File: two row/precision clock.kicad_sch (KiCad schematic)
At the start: 41 parts, among them J2 Barrel_Jack_Switch, Q1 2N5401, Q2 2N5401

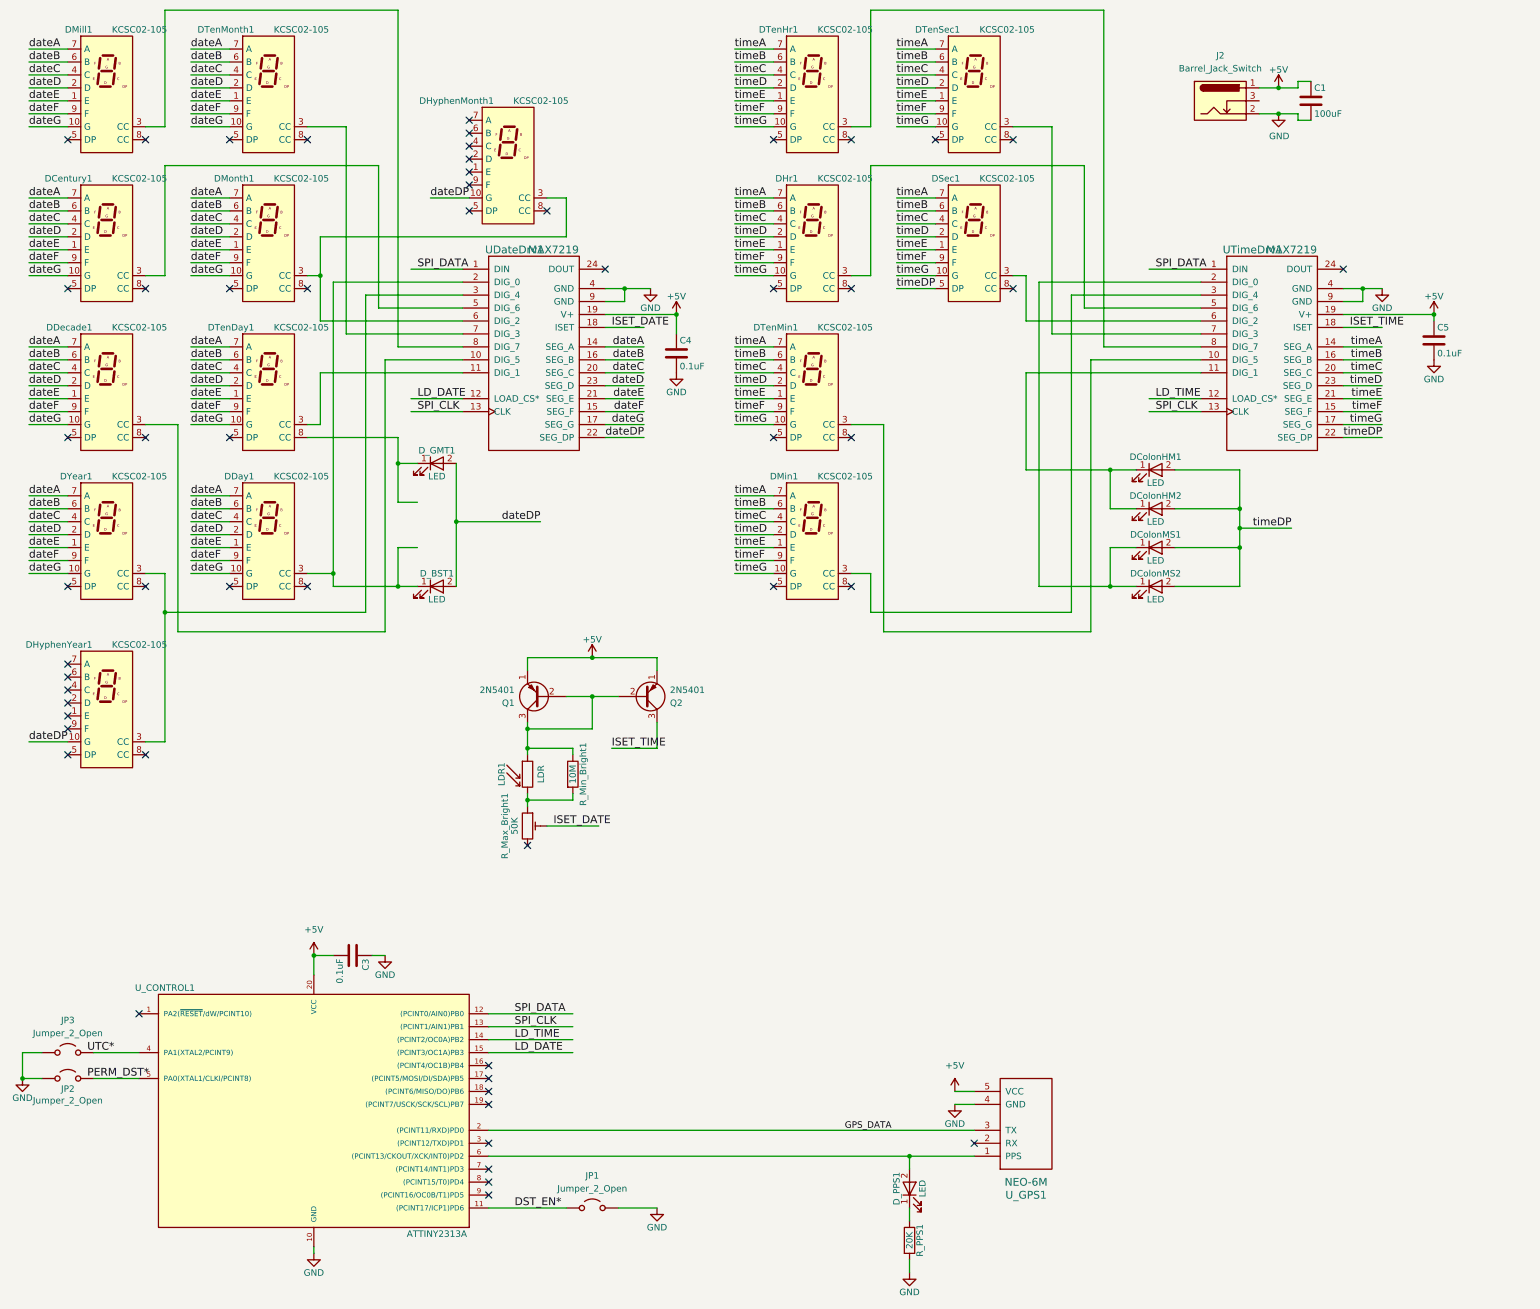
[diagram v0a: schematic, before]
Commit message: Rebuild two-row for 0.8" segments and improvements from prototype (1.0" are very difficult to source)
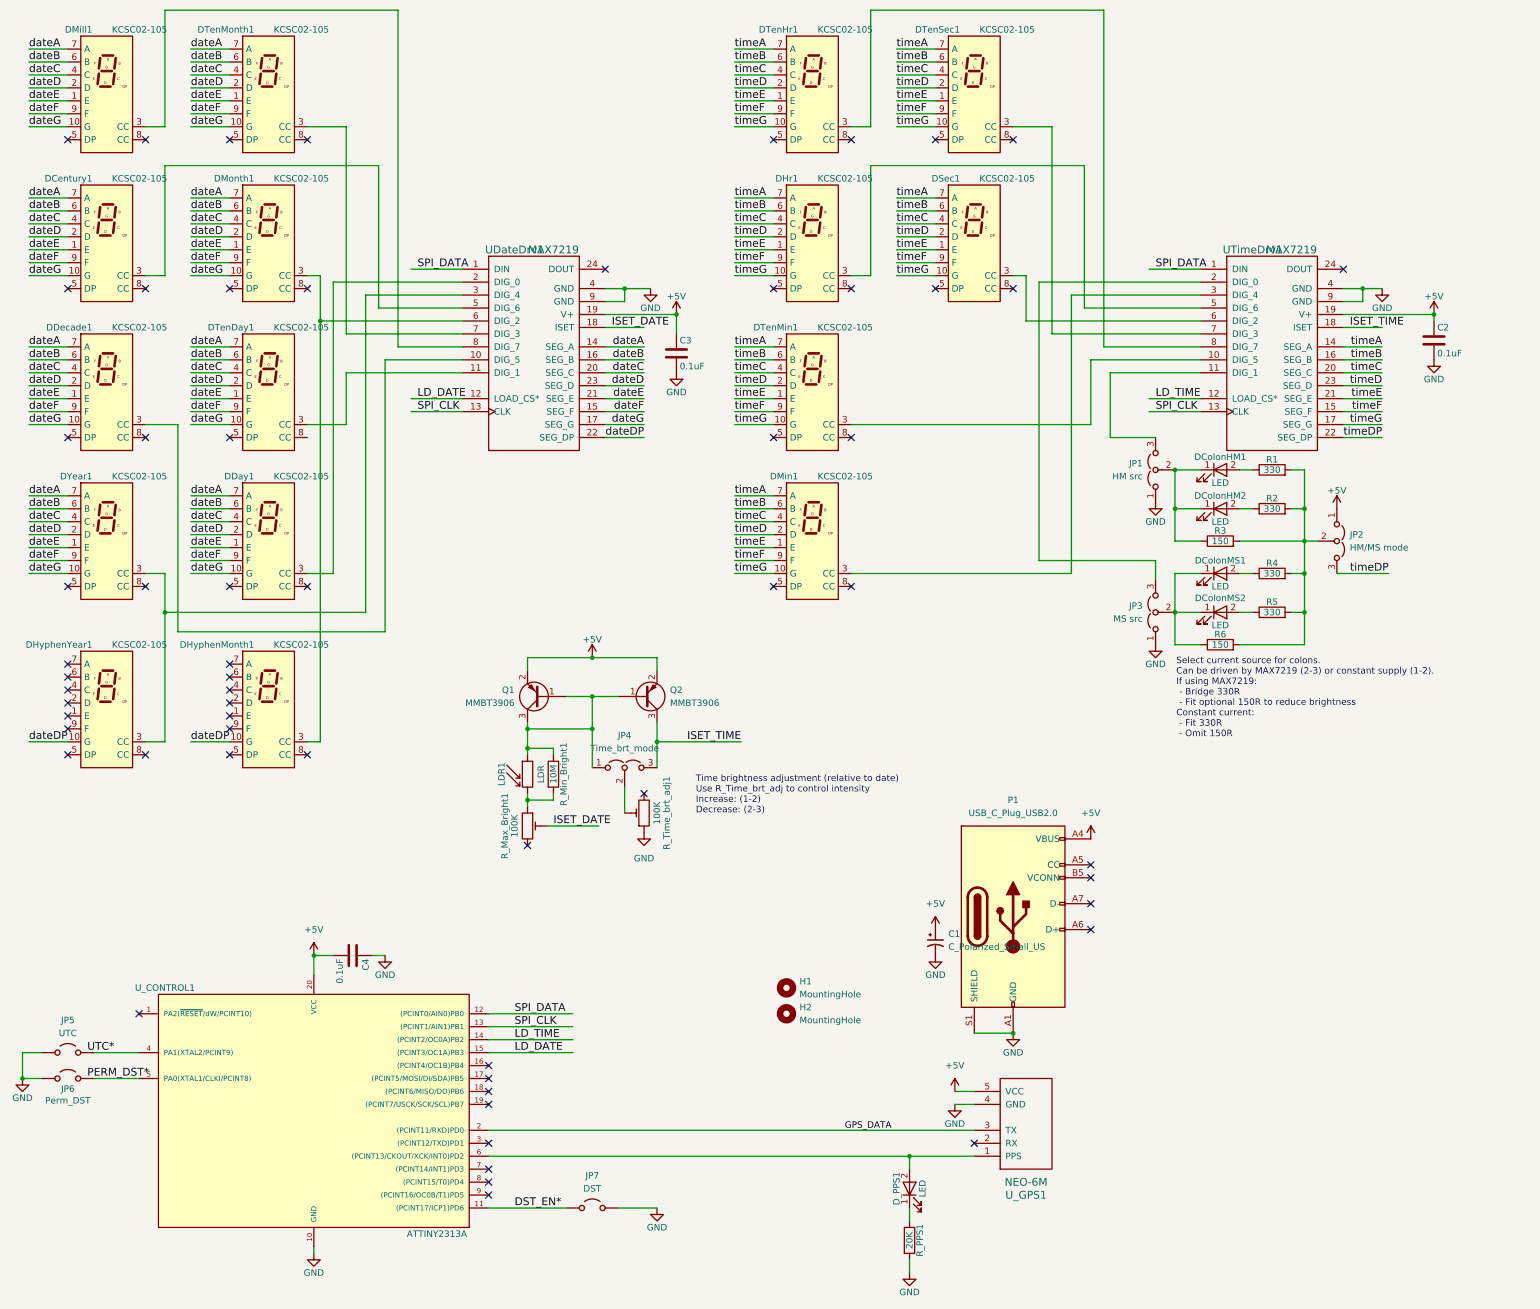
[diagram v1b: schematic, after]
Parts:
- removed C1: 100uF, Capacitor_THT:CP_Radial_D5.0mm_P2.50mm, symbol precision-clock-rescue:C
- removed D_BST1, D_GMT1: LED, LED_SMD:LED_1206_3216Metric, symbol precision-clock-rescue:LED
- removed J2: Barrel_Jack_Switch, Connector_BarrelJack:BarrelJack_Horizontal, symbol Connector:Barrel_Jack_Switch
- removed Q1, Q2: 2N5401, Package_TO_SOT_THT:TO-92_Inline_Wide, symbol precision-clock-rescue:Q_PNP_EBC
- added C1: C_Polarized_Small_US, Capacitor_THT:CP_Radial_D5.0mm_P2.50mm, symbol Device:C_Polarized_Small_US
- added H1: MountingHole, MountingHole:MountingHole_3.2mm_M3, symbol Mechanical:MountingHole
- added H2: MountingHole, MountingHole:MountingHole_2mm, symbol Mechanical:MountingHole
- added JP1: HM src, Jumper:SolderJumper-3_P1.3mm_Open_Pad1.0x1.5mm, symbol Jumper:Jumper_3_Open
- added JP2: HM/MS mode, Jumper:SolderJumper-3_P1.3mm_Open_Pad1.0x1.5mm, symbol Jumper:Jumper_3_Open
- added JP3: MS src, Jumper:SolderJumper-3_P1.3mm_Open_Pad1.0x1.5mm, symbol Jumper:Jumper_3_Open
- added JP4: Time_brt_mode, Connector_PinHeader_2.54mm:PinHeader_1x03_P2.54mm_Vertical, symbol Jumper:Jumper_3_Open
- added P1: USB_C_Plug_USB2.0, Connector_USB:USB_C_Receptacle_GCT_USB4125-xx-x_6P_TopMnt_Horizontal, symbol Connector:USB_C_Plug_USB2.0
- added Q1, Q2: MMBT3906, Package_TO_SOT_SMD:SOT-23, symbol Transistor_BJT:MMBT3906
- added R1, R2, R4, R5: 330, Resistor_SMD:R_1206_3216Metric, symbol precision-clock-rescue:R
- added R3, R6: 150, Resistor_SMD:R_1206_3216Metric, symbol precision-clock-rescue:R
- added R_Time_brt_adj1: 100K, Potentiometer_THT:Potentiometer_Piher_PT-6-V_Vertical, symbol precision-clock-rescue:POT_TRIM
- DHr1, DMin1, DSec1, DTenHr1, DTenMin1, DTenSec1: footprint precision clock:7seg1inchCC -> precision clock:7seg0.8CC
- JP5: renamed from JP3; value Jumper_2_Open -> UTC
- JP6: renamed from JP2; value Jumper_2_Open -> Perm_DST
- JP7: renamed from JP1; value Jumper_2_Open -> DST
- R_Max_Bright1: value 50K -> 100K
- U_GPS1: footprint Connector_PinHeader_2.54mm:PinHeader_1x05_P2.54mm_Vertical -> Connector_PinSocket_2.54mm:PinSocket_1x05_P2.54mm_Horizontal
- renumbered C5 to C2, C4 to C3, C3 to C4
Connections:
- net +5V: now also C1.1, JP2.1 (A), P1.A4 (VBUS), P1.A9 (VBUS), P1.B4 (VBUS), P1.B9 (VBUS), Q1.2 (E), Q2.2 (E)
- net GND: now also C1.2, JP1.1 (A), JP3.1 (A), P1.A1 (GND), P1.A12 (GND), P1.B1 (GND), P1.B12 (GND), P1.S1 (SHIELD), R_Time_brt_adj1.1
- net ISET_TIME: now also JP4.3 (B), Q2.3 (C)
- net timeDP: now also JP2.3 (B); no longer DColonHM1.2 (A), DColonHM2.2 (A), DColonMS1.2 (A), DColonMS2.2 (A), DSec1.5 (DP)
- net at DColonHM1.1 (K), DColonHM2.1 (K): now also JP1.2 (C), R3.1; no longer UTimeDrv1.11 (DIG_1)
- net at DColonMS1.1 (K), DColonMS2.1 (K): now also JP3.2 (C), R6.1; no longer UTimeDrv1.2 (DIG_0)
- net at LDR1.1, R_Min_Bright1.1: now also JP4.1 (A), Q1.1 (B), Q1.3 (C), Q2.1 (B)
- new net: JP1.3 (B), UTimeDrv1.11 (DIG_1)
- new net: JP3.3 (B), UTimeDrv1.2 (DIG_0)
- new net: DColonHM2.2 (A), R2.1
- new net: DColonMS1.2 (A), R4.1
- new net: DColonMS2.2 (A), R5.1
- new net: DColonHM1.2 (A), R1.1
- new net: JP2.2 (C), R1.2, R2.2, R3.2, R4.2, R5.2, R6.2
- new net: JP4.2 (C), R_Time_brt_adj1.2
- no-connect marks 55 -> 61
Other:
- note added: "Select current source for colons. Can be driven by MAX7219 (2-3) or constant supply (1-2). If using MAX7219: - Bridge 330R - Fit optional 150R to reduce brightness Constant current: - Fit 330R - Omit 150R"
- note added: "Time brightness adjustment (relative to date) Use R_Time_brt_adj to control intensity Increase: (1-2) Decrease: (2-3)"
- moved on the sheet: DColonHM1, DColonHM2, DColonMS1, DColonMS2, DHyphenMonth1, R_Min_Bright1

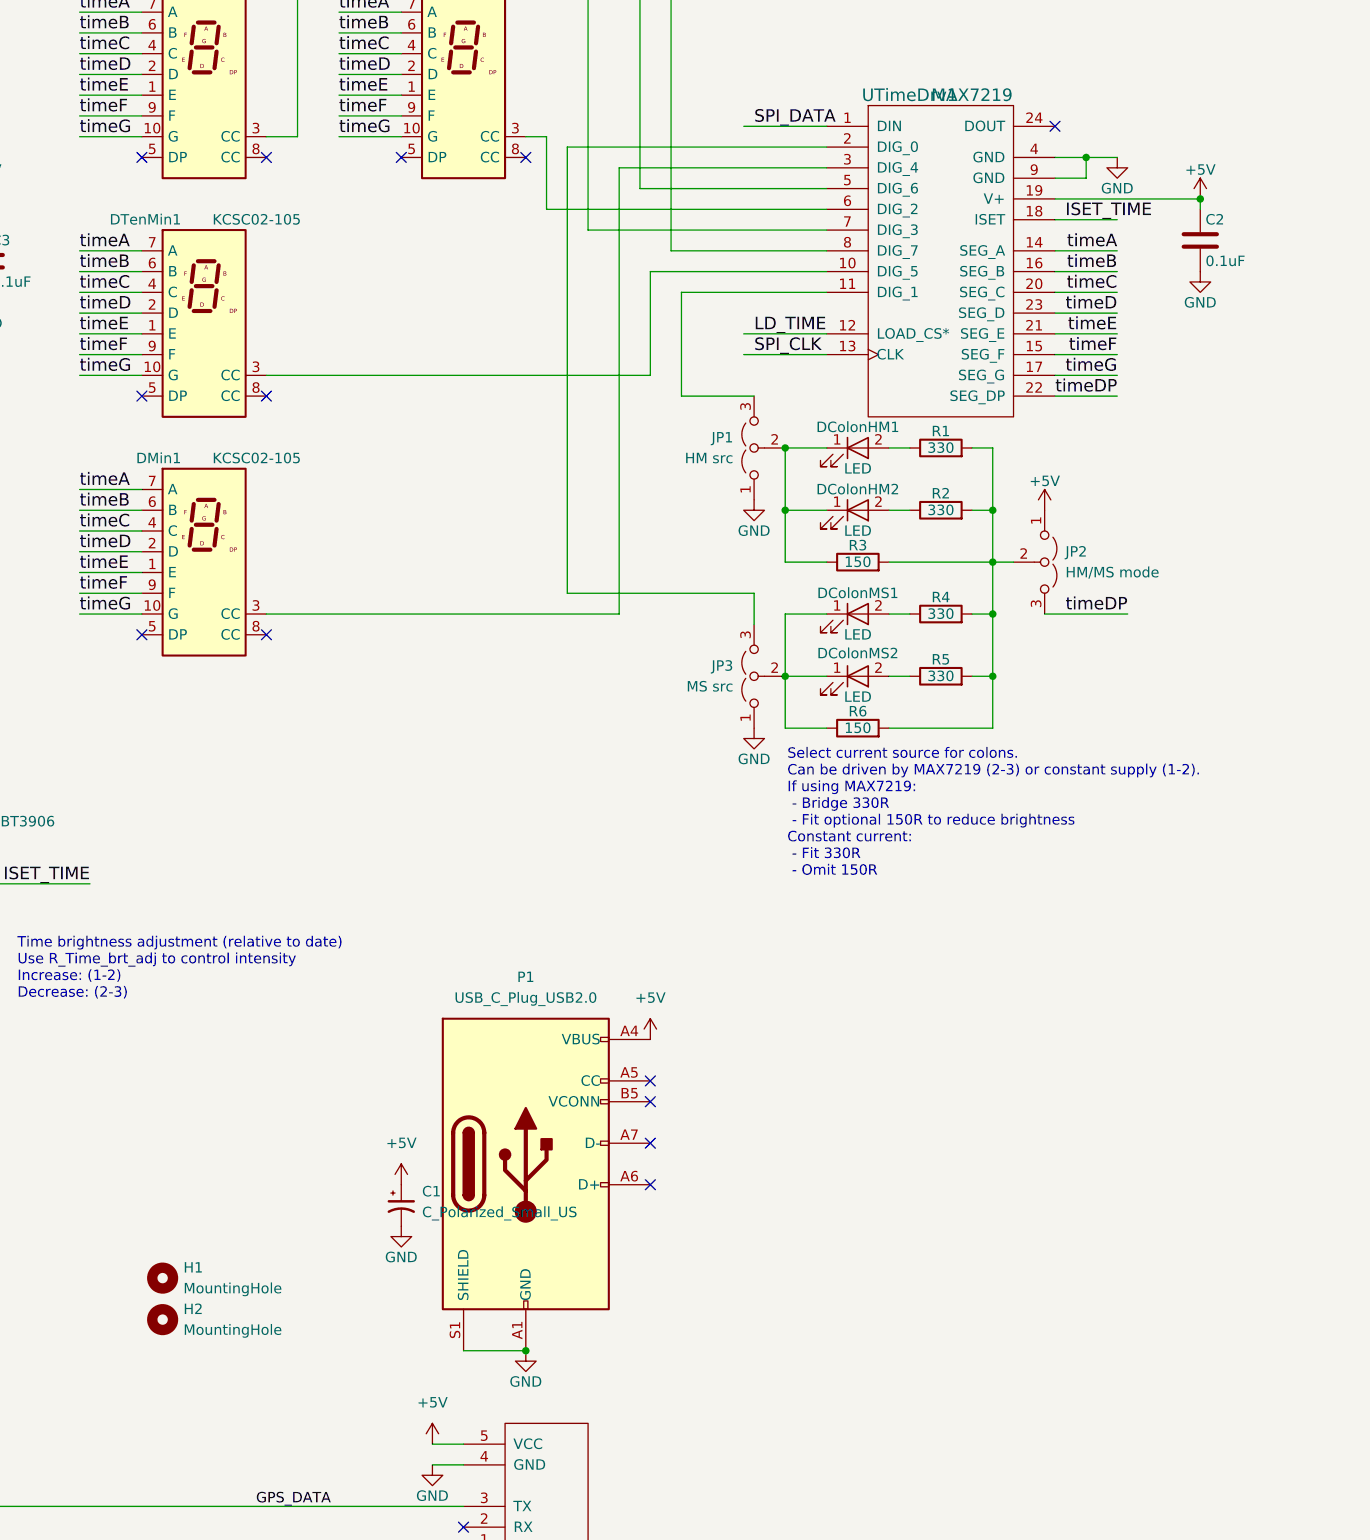
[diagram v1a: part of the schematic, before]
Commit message: Remove extra resistors, add second USB port location, cleanup trace routing
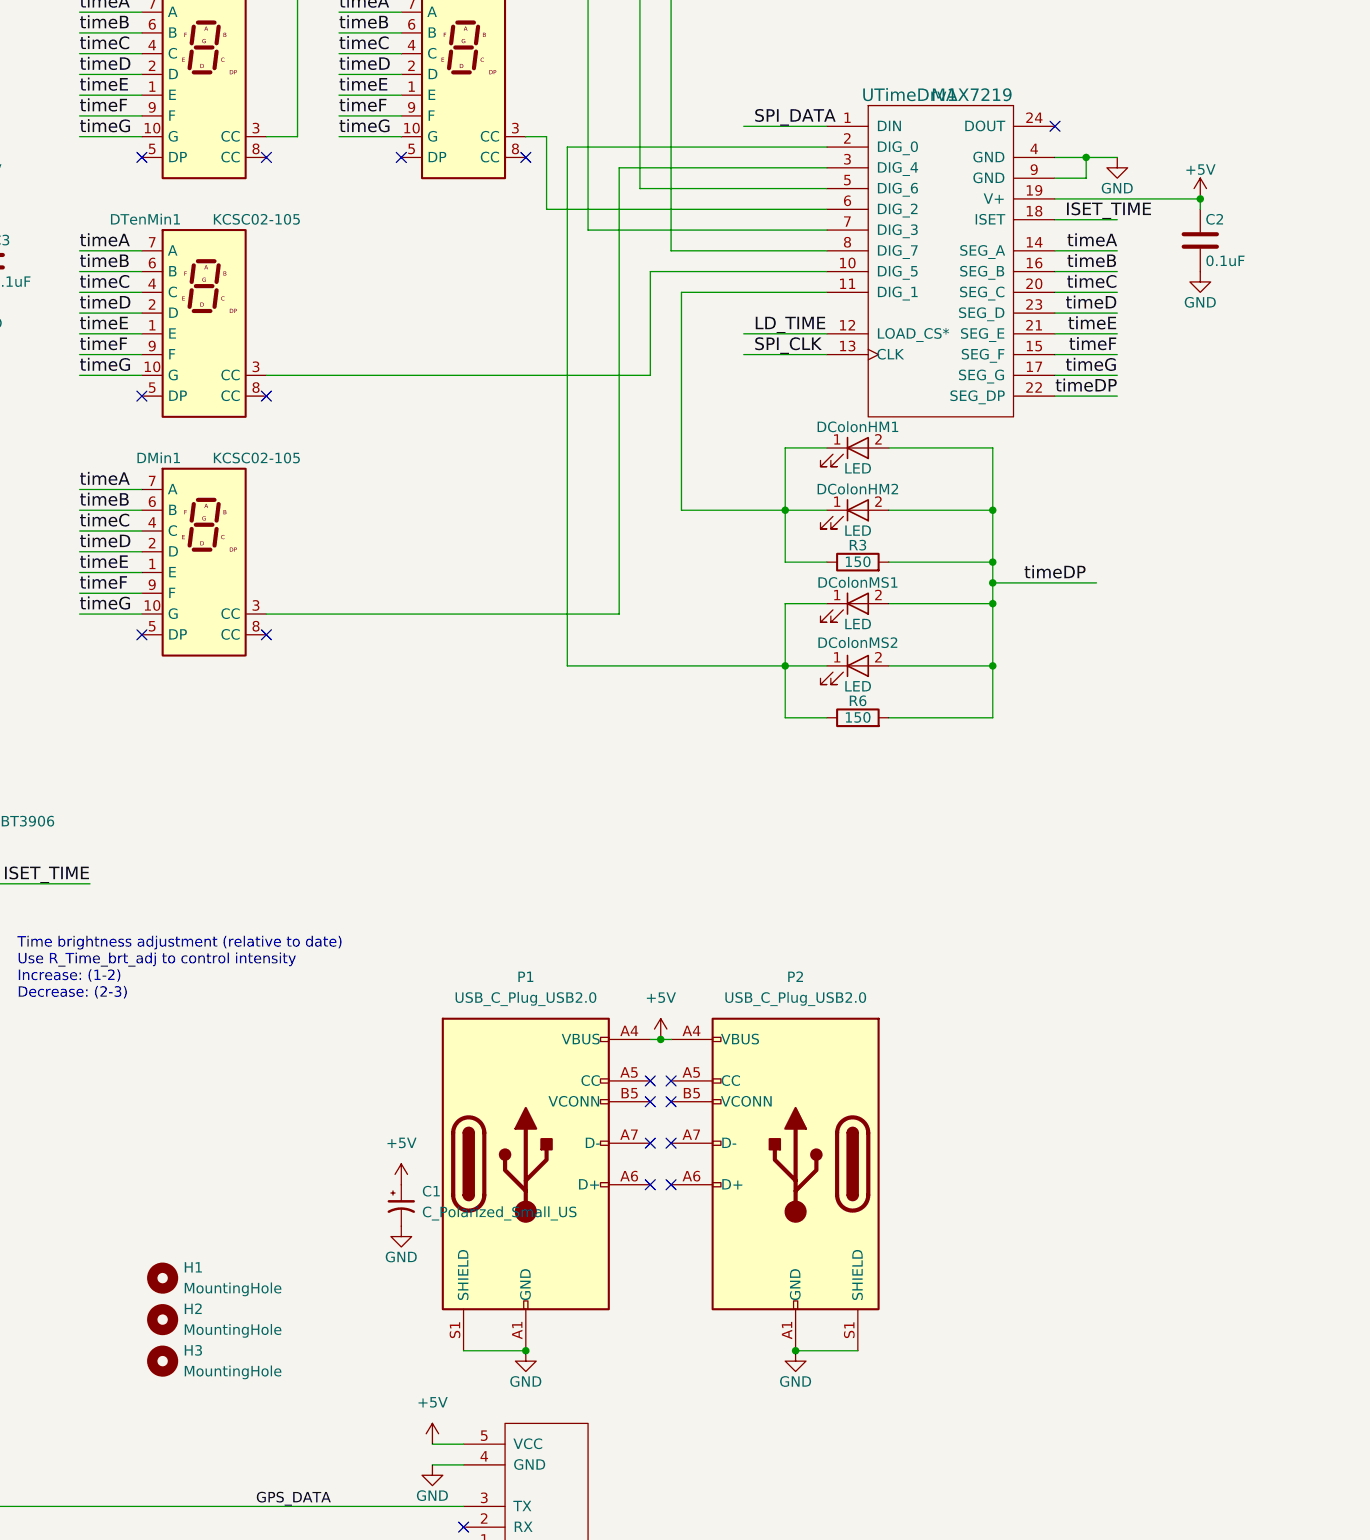
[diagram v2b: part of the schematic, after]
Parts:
- removed JP1: HM src, Jumper:SolderJumper-3_P1.3mm_Open_Pad1.0x1.5mm, symbol Jumper:Jumper_3_Open
- removed JP2: HM/MS mode, Jumper:SolderJumper-3_P1.3mm_Open_Pad1.0x1.5mm, symbol Jumper:Jumper_3_Open
- removed JP3: MS src, Jumper:SolderJumper-3_P1.3mm_Open_Pad1.0x1.5mm, symbol Jumper:Jumper_3_Open
- removed R1, R2, R4, R5: 330, Resistor_SMD:R_1206_3216Metric, symbol precision-clock-rescue:R
- added H3: MountingHole, MountingHole:MountingHole_2mm, symbol Mechanical:MountingHole
- added P2: USB_C_Plug_USB2.0, Connector_USB:USB_C_Receptacle_HRO_TYPE-C-31-M-17, symbol Connector:USB_C_Plug_USB2.0
- P1: footprint Connector_USB:USB_C_Receptacle_GCT_USB4125-xx-x_6P_TopMnt_Horizontal -> Connector_USB:USB_C_Receptacle_HRO_TYPE-C-31-M-17
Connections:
- net +5V: now also P2.A4 (VBUS), P2.A9 (VBUS), P2.B4 (VBUS), P2.B9 (VBUS)
- net GND: now also P2.A1 (GND), P2.A12 (GND), P2.B1 (GND), P2.B12 (GND), P2.S1 (SHIELD)
- net timeDP: now also DColonHM1.2 (A), DColonHM2.2 (A), DColonMS1.2 (A), DColonMS2.2 (A), R3.2, R6.2
- net at UTimeDrv1.11 (DIG_1): now also DColonHM1.1 (K), DColonHM2.1 (K), R3.1
- net at UTimeDrv1.2 (DIG_0): now also DColonMS1.1 (K), DColonMS2.1 (K), R6.1
- no-connect marks 61 -> 65
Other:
- note removed: "Select current source for colons. Can be driven by MAX7219 (2-3) or constant supply (1-2). If using MAX7219: - Bridge 330R - Fit optional 150R to reduce brightness Constant current: - Fit 330R - Omit 150R"
- moved on the sheet: DColonMS1, DColonMS2, R6
